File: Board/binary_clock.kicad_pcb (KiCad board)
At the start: 2 copper layers, 111.8 x 71.1 mm, 75 parts, among them J1 Conn_01x02, SW1 SW_SPST_LED, SW2 SW_Push, SW3 SW_Push, SW4 SW_Push, SW5 SW_Push, U1 OKI-78SR-3.3_1.5-W36H-C, U10 4071, U11 4071, U2 CD4060BE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

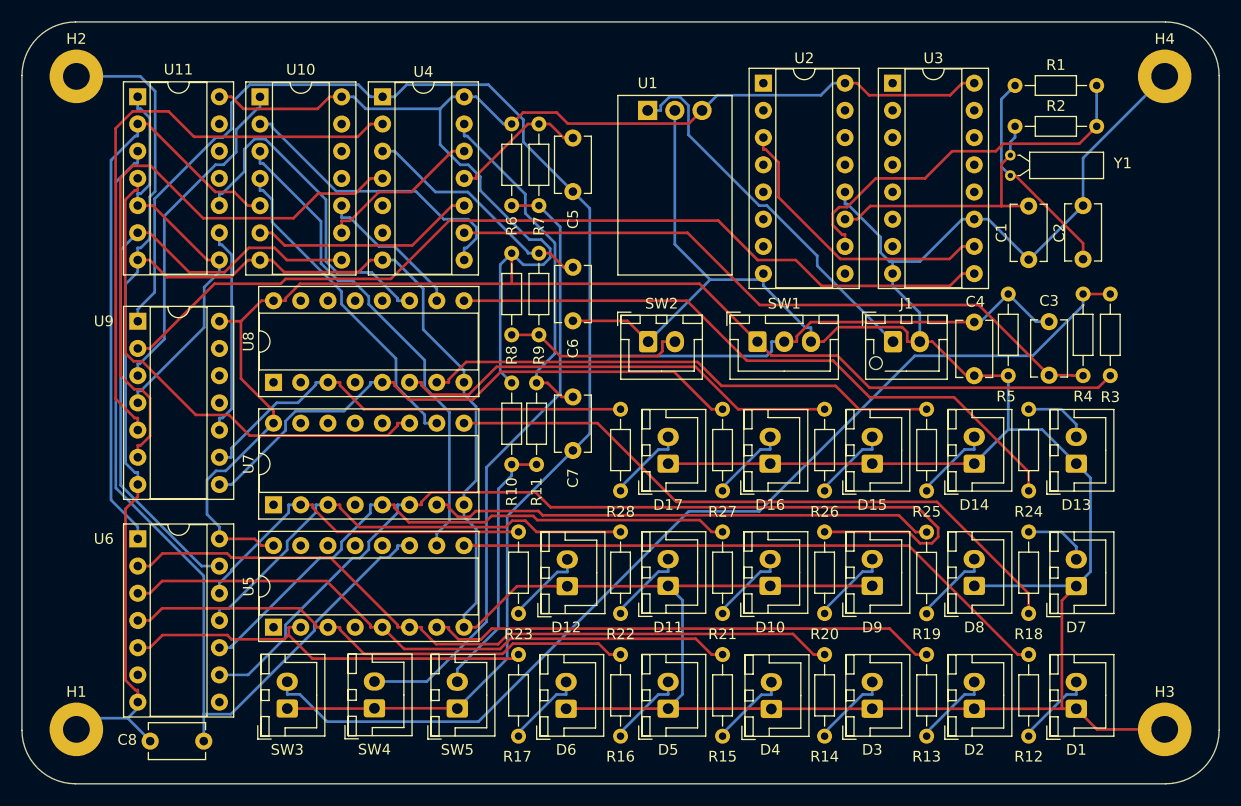
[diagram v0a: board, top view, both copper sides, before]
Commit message: fix 3.3v regulator footprint
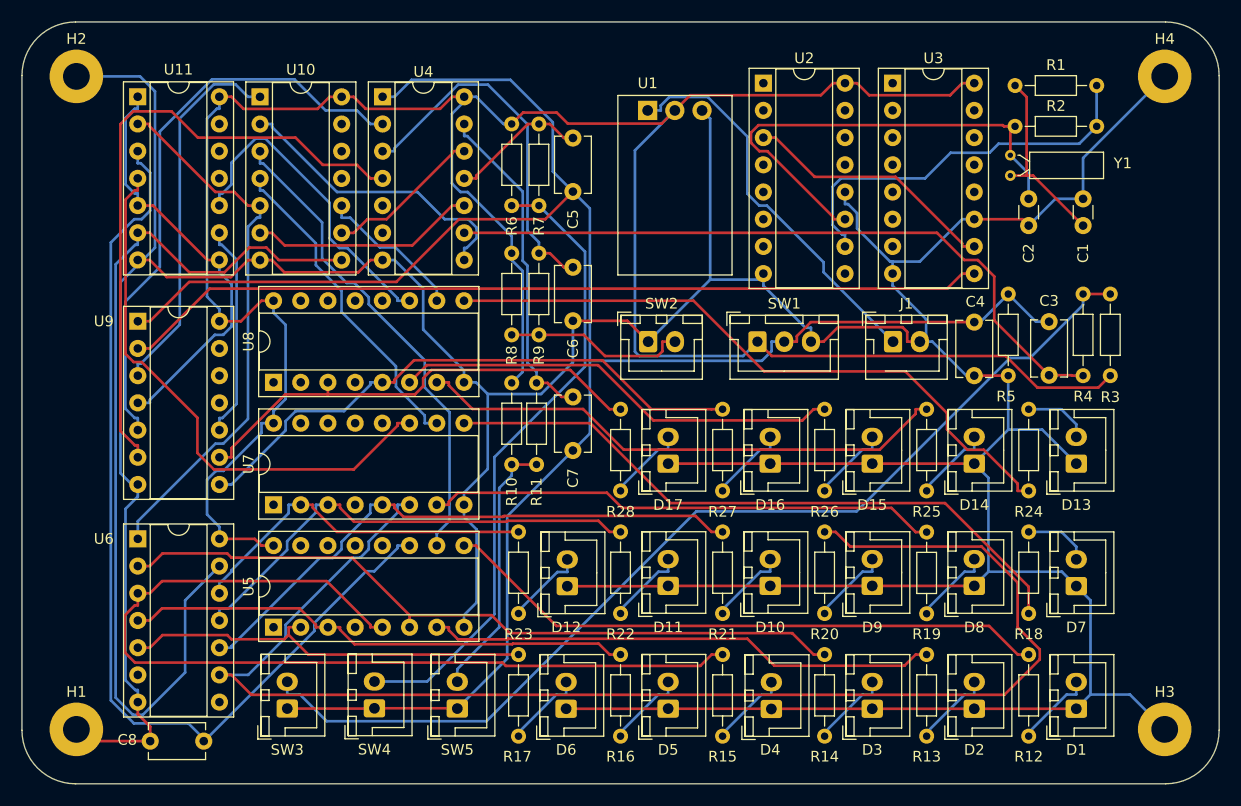
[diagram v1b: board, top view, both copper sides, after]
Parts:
- C1, C2: footprint Capacitor_THT:C_Disc_D5.1mm_W3.2mm_P5.00mm -> Capacitor_THT:C_Disc_D3.0mm_W1.6mm_P2.50mm
- moved C1 3.14 mm to (182.9, 85.0)
- moved C2 0.67 mm to (177.8, 82.5)
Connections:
- U1 pad 2: GND -> +3.3V
- U1 pad 3: +3.3V -> GND
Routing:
- net Net-(U7-Q2): track 89.4 -> 132.6 mm
- net Net-(U5-Q3): track 58.8 -> 88.1 mm
- net /Clock_Binary/CARRY_MIN: track 58.6 -> 86.4 mm
- net Net-(U2-(PHI)I): track 25.6 -> 45.3 mm
- net Net-(C6-Pad1): track 22.3 -> 34.0 mm
- net /Interface/SWITCH_PAUSE_NOT: track 180.3 -> 188.3 mm
- net /Clock_Binary/RESET_SEC: track 85.8 -> 91.5 mm
- net /Clock_1hz/CLK_1Hz: track 86.0 -> 81.0 mm
- net /Clock_Binary/RESET_MIN: track 47.3 -> 51.9 mm
- net /Clock_Binary/CARRY_SEC: track 55.7 -> 51.1 mm
- net +3.3V: track 235.9 -> 239.6 mm
- net Net-(U10-Pad1): track 31.5 -> 35.1 mm
- net /Clock_1hz/CLK_2Hz: track 27.4 -> 24.1 mm
- net /Interface/BUTTON_RESET: track 56.8 -> 59.5 mm
- net Net-(C1-Pad1): track 20.2 -> 17.6 mm
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
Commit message: add caps to all resets
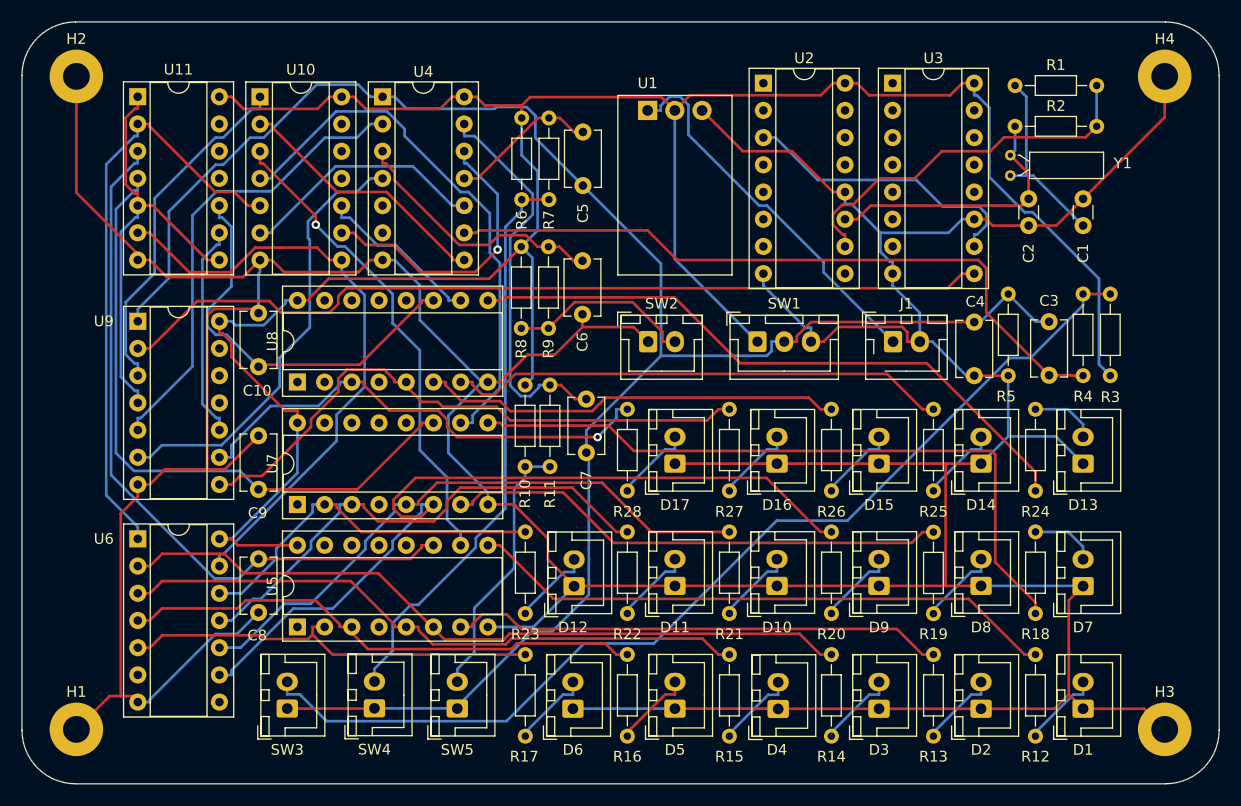
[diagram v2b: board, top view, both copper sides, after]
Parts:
- added C10: 100nf, Capacitor_THT:C_Disc_D5.1mm_W3.2mm_P5.00mm, F.Cu at (105.9, 98.2)
- added C9: 100nf, Capacitor_THT:C_Disc_D5.1mm_W3.2mm_P5.00mm, F.Cu at (105.9, 109.7)
- moved C8 17.8 mm to (105.9, 116.2), turned to -90 degrees
- moved U5 2.23 mm to (109.5, 122.5)
- moved U7 2.23 mm to (109.5, 111.1)
- moved U8 2.23 mm to (109.5, 99.7)
- moved C7 1.27 mm to (136.5, 101.2)
- moved R10 1.27 mm to (130.8, 99.9)
- moved R11 1.27 mm to (133.1, 107.6)
- moved C5 1.09 mm to (136.2, 76.3)
- moved R6 1.09 mm to (130.5, 75.0)
- moved R7 1.09 mm to (133.0, 82.6)
- moved C6 1.08 mm to (136.1, 88.3)
- moved R8 1.08 mm to (130.4, 87.0)
- moved R9 1.08 mm to (133.0, 94.6)
- moved D10 0.64 mm to (154.3, 118.7)
- moved D12 0.64 mm to (135.4, 118.7)
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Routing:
- net Net-(U7-Q2): track 132.6 -> 76.8 mm
- net /Clock_Binary/CARRY_MIN: track 86.4 -> 57.3 mm
- net Net-(U5-Q3): track 88.1 -> 59.3 mm
- net /Clock_Binary/RESET_SEC: track 91.5 -> 66.9 mm
- net /Clock_Binary/CLOCK_MIN: track 30.5 -> 50.7 mm
- net Net-(U2-(PHI)I): track 45.3 -> 25.6 mm
- net /Interface/BUTTON_RESET: track 59.5 -> 41.3 mm
- net GND: track 453.4 -> 468.7 mm
- net /Interface/BUTTON_HOUR: track 14.7 -> 27.6 mm, vias 0 -> 1
- net +3.3V: track 239.6 -> 228.5 mm
- net /Interface/SWITCH_PAUSE: track 54.4 -> 43.6 mm
- net /Interface/SWITCH_PAUSE_NOT: track 188.3 -> 177.6 mm
- net Net-(C6-Pad1): track 34.0 -> 24.8 mm
- net /Clock_Binary/RESET_MIN: track 51.9 -> 60.4 mm
- net /Clock_Binary/RESET_HOUR: track 30.5 -> 38.2 mm
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
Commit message: add branding and version silkscreen
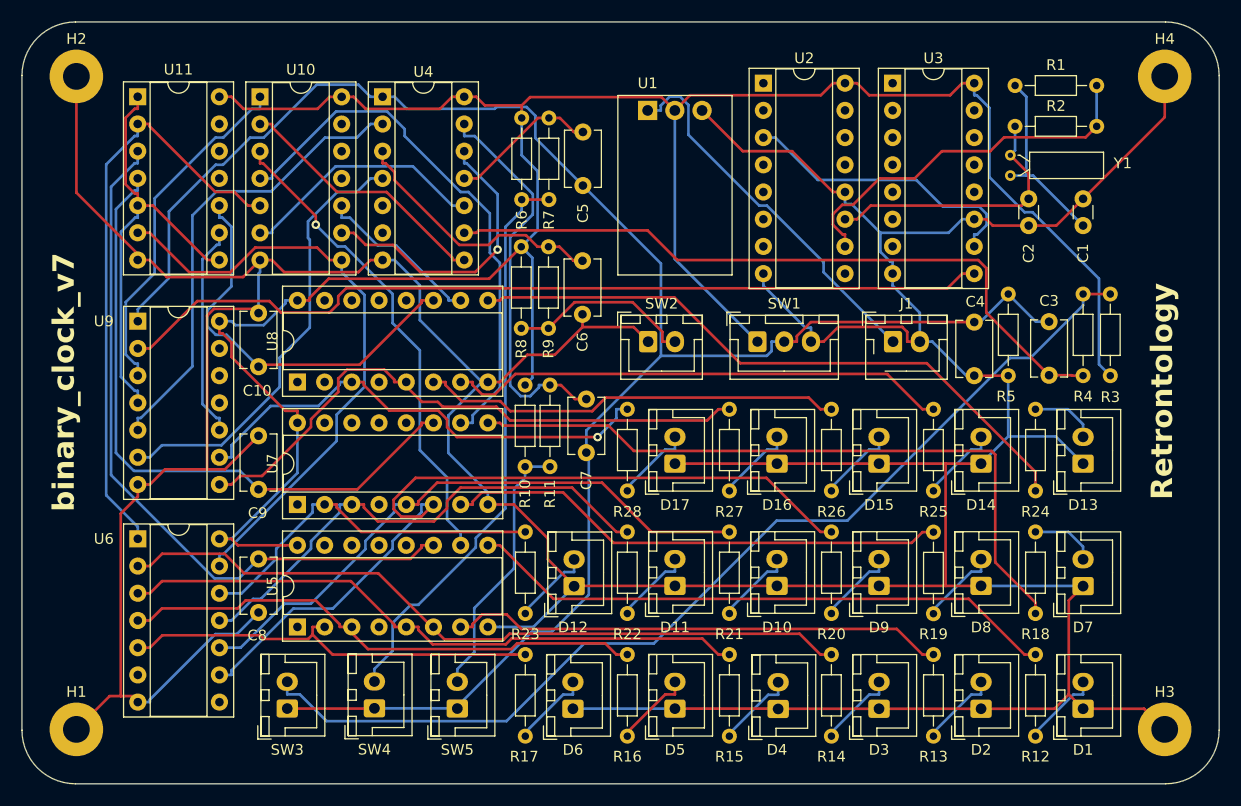
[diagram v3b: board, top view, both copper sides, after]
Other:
- board text added: "Retrontology"
- board text added: "binary_clock_v7"
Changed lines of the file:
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@@
   (gr_arc (start 190.58 66.04) (mid 194.115534 67.504466) (end 195.58 71.04)
     (stroke (width 0.1) (type default)) (layer "Edge.Cuts"))
+  (gr_text "Retrontology" (at 191.426735 110.646107 90) (layer "F.SilkS")
+    (effects (font (size 2 2) (thickness 0.2) bold) (justify left bottom))
+  )
+  (gr_text "binary_clock_v7" (at 88.9 111.76 90) (layer "F.SilkS")
+    (effects (font (size 2 2) (thickness 0.2) bold) (justify left bottom))
+  )
   (gr_text "MountingHole_Pad" (at 168.91 71.755) (layer "F.Fab")
     (effects (font (size 1 1) (thickness 0.15)))
